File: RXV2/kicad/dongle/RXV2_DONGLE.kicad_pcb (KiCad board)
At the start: 2 copper layers, 23.5 x 36 mm, 2 parts, among them J1 to Nexus port, U1 XIAO ESP32-S3

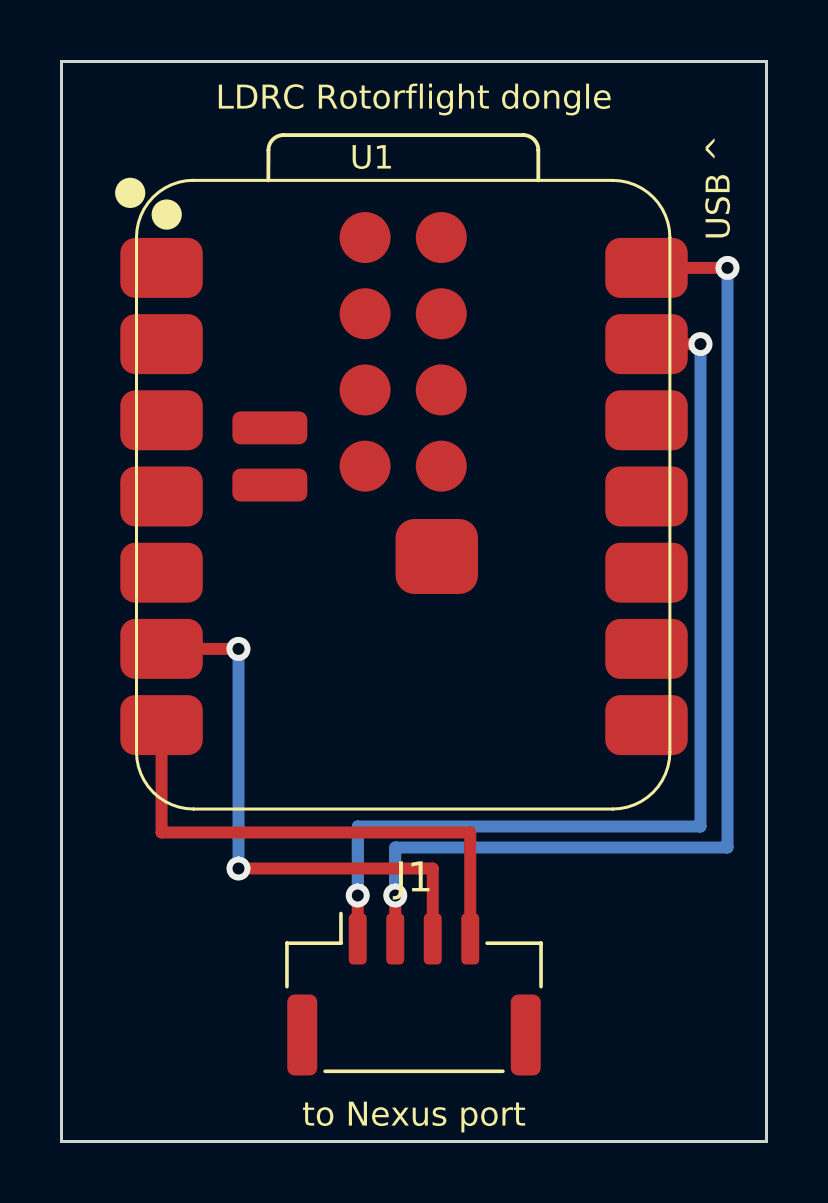
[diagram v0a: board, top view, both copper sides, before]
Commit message: RXV2 dongle PCB v2: XIAO-sized, connector on the back, receiver's pin order
20.9 x 24.2 mm. JST GH under the module with the opening at the bottom
edge; pins 1 GND, 2 +5V, 3 TX (D6), 4 RX (D5) exactly as the receiver
board's J1, so a 1:1 pigtail plugs in. DRC clean.

Co-Authored-By: Claude Fable 5.1 <noreply@anthropic.com>
Claude-Session: https://claude.ai/code/session_01DvvNNevU4xtNTYtdVBAM7h
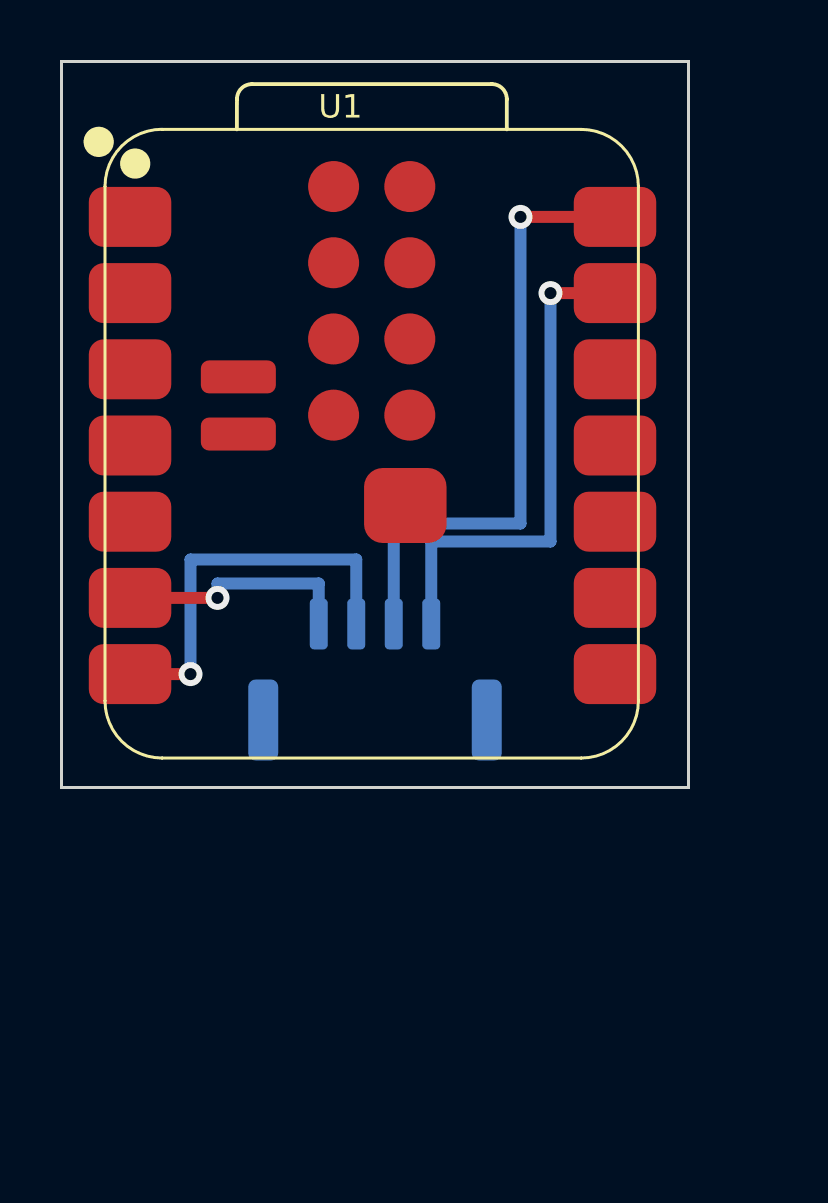
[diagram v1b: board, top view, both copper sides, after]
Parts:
- J1: value to Nexus port -> Nexus port; moved to B.Cu
- U1: footprint XIAO-ESP32-S3-SMD_PAD -> XIAO-ESP32-S3-SMD
- moved J1 10.6 mm to (10.4, 20.6), turned to 180 degrees
- moved U1 2.00 mm to (1.45, 23.3)
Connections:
- net 5V renamed +5V
- J1 pad 3: FC_TX -> TX
- J1 pad 4: FC_RX -> RX
- U1 pad 6: FC_TX -> RX
- U1 pad 7: FC_RX -> TX
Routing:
- net FC_TX: track 18.7 -> 0.00 mm, vias 2 -> 0
- net FC_RX: track 17.4 -> 0.00 mm
- net GND: track 33.1 -> 17.2 mm, vias 2 -> 1
- net +5V: track 36.1 -> 20.9 mm, vias 2 -> 1
- net TX: track 0.00 -> 13.5 mm, vias 0 -> 1
- net RX: track 0.00 -> 8.12 mm, vias 0 -> 1
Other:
- board size 23.5 x 36 mm -> 20.9 x 24.2 mm
- board text removed: "to Nexus port"
